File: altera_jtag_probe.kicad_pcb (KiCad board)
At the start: 2 copper layers, 38.1 x 19 mm, 2 parts

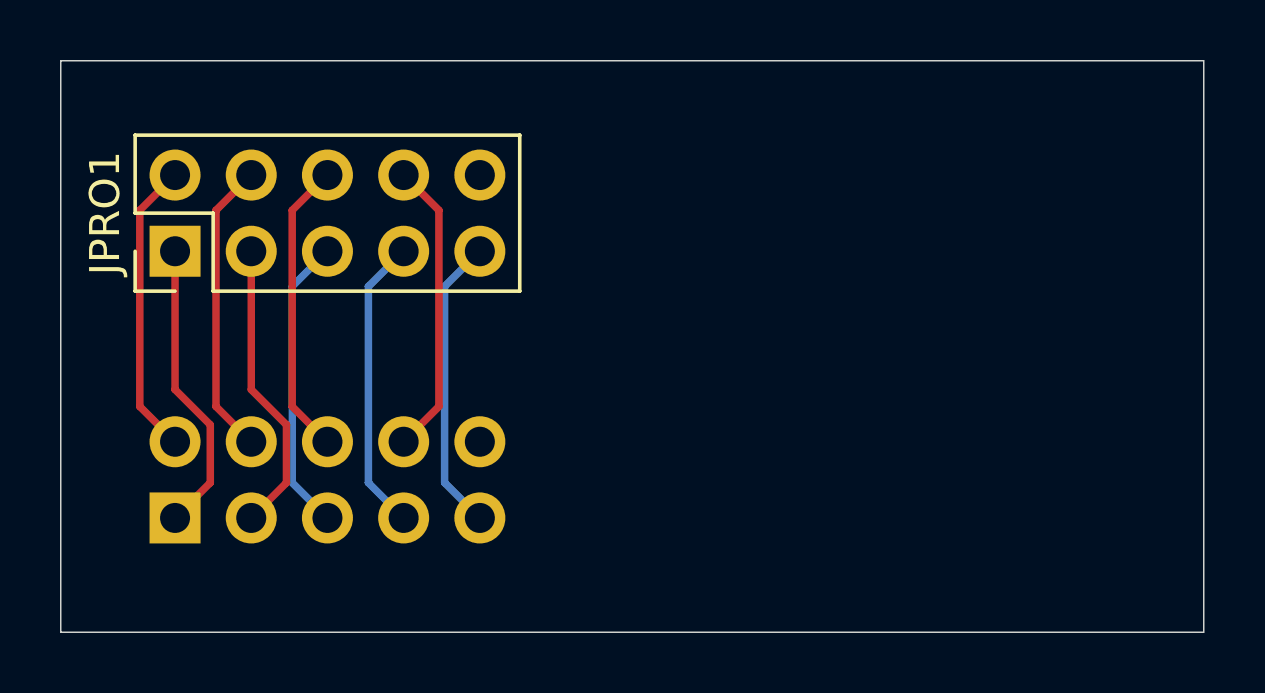
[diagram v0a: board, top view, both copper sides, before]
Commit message: trim size, traces are 0.3 mm instead of 0.25 mm
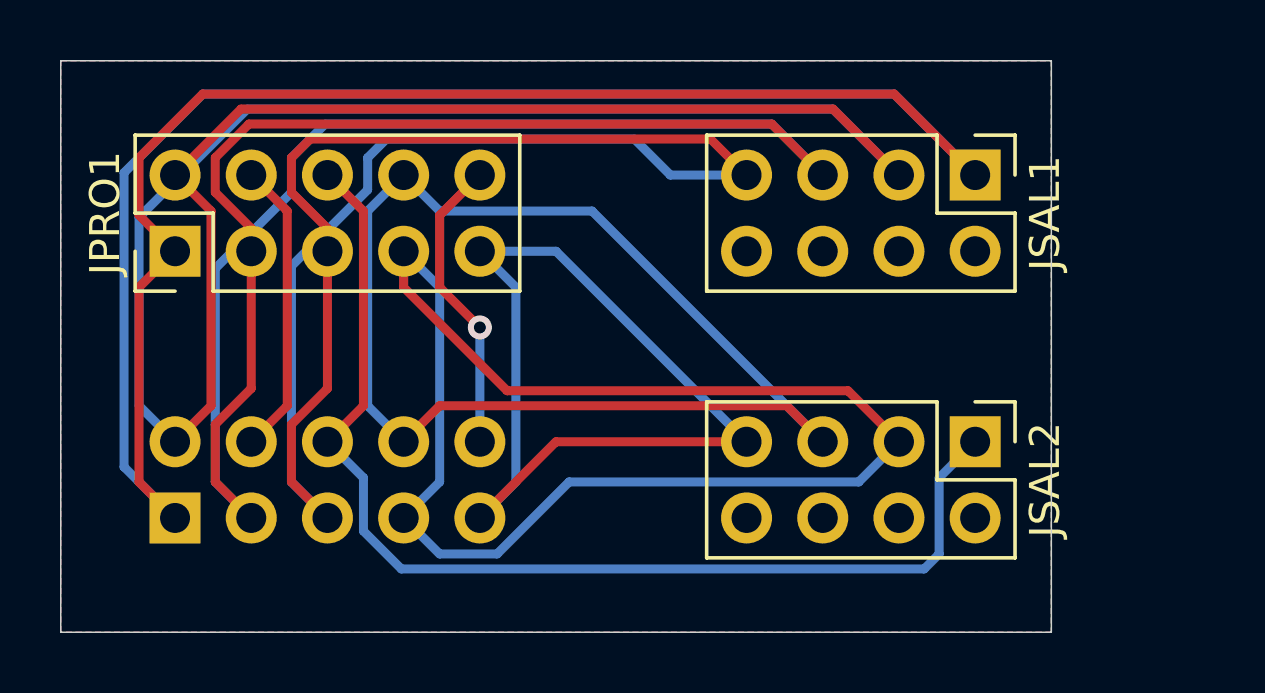
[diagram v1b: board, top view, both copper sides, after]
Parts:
- added JSAL1: Conn_02x04_Odd_Even, Connector_PinHeader_2.54mm:PinHeader_2x04_P2.54mm_Vertical, F.Cu at (144.8, 99.1)
- added JSAL2: Conn_02x04_Odd_Even, Connector_PinHeader_2.54mm:PinHeader_2x04_P2.54mm_Vertical, F.Cu at (144.8, 108.0)
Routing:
- net Net-(JBRD1-Pad1): track 9.86 -> 86.2 mm
- net Net-(JBRD1-Pad2): track 9.86 -> 71.6 mm
- net Net-(JBRD1-Pad3): track 9.86 -> 67.4 mm
- net Net-(JBRD1-Pad5): track 9.86 -> 56.4 mm
- net Net-(JBRD1-Pad7): track 9.86 -> 48.9 mm
- net Net-(JBRD1-Pad8): track 9.86 -> 42.5 mm
- net Net-(JBRD1-Pad6): track 9.86 -> 37.5 mm
- net Net-(JBRD1-Pad9): track 9.86 -> 31.3 mm
- net GND: track 0.00 -> 10.0 mm, vias 0 -> 1
- added copper zone on B.Cu, net GND
- added copper zone on F.Cu, net GND
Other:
- board size 38.1 x 19 mm -> 33 x 19 mm
